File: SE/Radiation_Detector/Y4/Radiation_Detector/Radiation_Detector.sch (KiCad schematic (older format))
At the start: 12 parts, among them IC1 MICROFJ-60035-TSV-TR1, J1 Bus

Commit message: changed it so that there was 1 more level of heigherarchy now it's the top level with the bus connected to the bias and 4 detectors
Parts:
- removed C2: 10 nF (HV), symbol 001:C
- removed C3: 1 uF, symbol 001:C
- removed IC1: MICROFJ-60035-TSV-TR1, SS:SiPM_BGA36C100P6X6_613X613X67, symbol SS:MICROFJ-60035-TSV-TR1
- removed R6: 1 k, symbol Device:R_US
- removed R7: 108 k, symbol Device:R_US
- J1: symbol SS:Bus -> Radiation_Detector-rescue:Bus-SS
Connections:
- net labels removed: PS-A2D
- wire segments 125 -> 52
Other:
- note added: "Det_1"
- note added: "Det_2"
- note added: "Det_3"
- note added: "Det_4\n"
- note removed: "Charge\nSensitive\nPreamplifier"
- note removed: "Pulse\nShaper"
- note removed: "SiPM"

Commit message: incorporated A2D with SiPM, main work continueing from here is the Detector schematic and maybe the A2D references. in the Detector the SiPM needs to be changed to the Broadcom SiPM and the CSP needs to be the redesigned one and the PS needs to be designed so that we can redesign the Cremat one
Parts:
- J1: symbol Radiation_Detector-rescue:Bus-SS -> SS:Bus
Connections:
- wire segments 52 -> 56
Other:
- note added: "A2D_1"
- note added: "A2D_2\n"
- note added: "A2D_3"
- note added: "A2D_4"
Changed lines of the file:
@@
 $Descr A4 11693 8268
 encoding utf-8
-Sheet 1 4
+Sheet 1 17
 Title ""
 Date ""
@@
 $EndDescr
 $Comp
-L Radiation_Detector-rescue:Bus-SS J1
+L SS:Bus J1
 U 1 1 5EBBBD0C
 P 1350 2000
@@
 S 4850 800  1050 800
 U 5EBD2B15
-F0 "Detector_1" 50
-F1 "Detector_1.sch" 50
+F0 "Det_1" 50
+F1 "Detector.sch" 50
 F2 "+30V_Bias" I L 4850 1000 50
 F3 "+8V" I L 4850 1200 50
@@
 Text Notes 5100 1250 0    100  ~ 20
 Det_1
+Text Notes 5100 2250 0    100  ~ 20
+Det_2
+Text Notes 5100 3250 0    100  ~ 20
+Det_3
+Text Notes 5100 4250 0    100  ~ 20
+Det_4\n
+Connection ~ 4250 1000
+Wire Wire Line
+	4250 1000 4250 1200
+Wire Wire Line
+	4450 1000 4450 2000
+Connection ~ 4450 1000
+Wire Wire Line
+	4450 1000 4250 1000
+Connection ~ 4450 3000
+Wire Wire Line
+	4450 3000 4450 4000
+Connection ~ 4450 2000
+Wire Wire Line
+	4450 2000 4450 3000
+Text GLabel 4750 1200 0    50   Input ~ 0
++8V
+Wire Wire Line
+	4450 1000 4850 1000
+Wire Wire Line
+	4850 1200 4750 1200
+Text GLabel 4750 1400 0    50   Input ~ 0
+GND
+Wire Wire Line
+	4750 1400 4850 1400
+Wire Wire Line
+	4450 2000 4850 2000
+Wire Wire Line
+	4450 3000 4850 3000
+Wire Wire Line
+	4450 4000 4850 4000
+Text GLabel 4750 2200 0    50   Input ~ 0
++8V
+Wire Wire Line
+	4850 2200 4750 2200
+Text GLabel 4750 2400 0    50   Input ~ 0
+GND
+Wire Wire Line
+	4750 2400 4850 2400
+Text GLabel 4750 3200 0    50   Input ~ 0
++8V
+Wire Wire Line
+	4850 3200 4750 3200
+Text GLabel 4750 3400 0    50   Input ~ 0
+GND
+Wire Wire Line
+	4750 3400 4850 3400
+Text GLabel 4750 4200 0    50   Input ~ 0
++8V
+Wire Wire Line
+	4850 4200 4750 4200
+Text GLabel 4750 4400 0    50   Input ~ 0
+GND
+Wire Wire Line
+	4750 4400 4850 4400
 $Sheet
 S 4850 1800 1050 800
-U 5EC023EE
-F0 "sheet5EC023E8" 50
-F1 "Detector_1.sch" 50
+U 5EC10E33
+F0 "Det_2" 50
+F1 "Detector.sch" 50
 F2 "+30V_Bias" I L 4850 2000 50
 F3 "+8V" I L 4850 2200 50
@@
 F5 "PS-A2D" I R 5900 2200 50
 $EndSheet
-Text Notes 5100 2250 0    100  ~ 20
-Det_2
 $Sheet
 S 4850 2800 1050 800
-U 5EC027A1
-F0 "sheet5EC0279B" 50
-F1 "Detector_1.sch" 50
+U 5EC116B0
+F0 "Det_3" 50
+F1 "Detector.sch" 50
 F2 "+30V_Bias" I L 4850 3000 50
 F3 "+8V" I L 4850 3200 50
@@
 F5 "PS-A2D" I R 5900 3200 50
 $EndSheet
-Text Notes 5100 3250 0    100  ~ 20
-Det_3
 $Sheet
 S 4850 3800 1050 800
-U 5EC02B54
-F0 "sheet5EC02B4E" 50
-F1 "Detector_1.sch" 50
+U 5EC11F15
+F0 "Det_4" 50
+F1 "Detector.sch" 50
 F2 "+30V_Bias" I L 4850 4000 50
 F3 "+8V" I L 4850 4200 50
@@
 F5 "PS-A2D" I R 5900 4200 50
 $EndSheet
-Text Notes 5100 4250 0    100  ~ 20
-Det_4\n
-Connection ~ 4250 1000
-Wire Wire Line
-	4250 1000 4250 1200
-Wire Wire Line
-	4450 1000 4450 2000
-Connection ~ 4450 1000
-Wire Wire Line
-	4450 1000 4250 1000
-Connection ~ 4450 3000
-Wire Wire Line
-	4450 3000 4450 4000
-Connection ~ 4450 2000
-Wire Wire Line
-	4450 2000 4450 3000
-Text GLabel 4750 1200 0    50   Input ~ 0
-+8V
-Wire Wire Line
-	4450 1000 4850 1000
-Wire Wire Line
-	4850 1200 4750 1200
-Text GLabel 4750 1400 0    50   Input ~ 0
-GND
-Wire Wire Line
-	4750 1400 4850 1400
-Wire Wire Line
-	4450 2000 4850 2000
-Wire Wire Line
-	4450 3000 4850 3000
-Wire Wire Line
-	4450 4000 4850 4000
-Text GLabel 4750 2200 0    50   Input ~ 0
-+8V
-Wire Wire Line
-	4850 2200 4750 2200
-Text GLabel 4750 2400 0    50   Input ~ 0
-GND
-Wire Wire Line
-	4750 2400 4850 2400
-Text GLabel 4750 3200 0    50   Input ~ 0
-+8V
-Wire Wire Line
-	4850 3200 4750 3200
-Text GLabel 4750 3400 0    50   Input ~ 0
-GND
-Wire Wire Line
-	4750 3400 4850 3400
-Text GLabel 4750 4200 0    50   Input ~ 0
-+8V
-Wire Wire Line
-	4850 4200 4750 4200
-Text GLabel 4750 4400 0    50   Input ~ 0
-GND
-Wire Wire Line
-	4750 4400 4850 4400
+$Sheet
+S 6100 1100 1100 700
+U 5EBDE6C5
+F0 "A2D_1" 50
+F1 "A2D.sch" 50
+F2 "PS-A2D" I L 6100 1200 50
+F3 "S1" I R 7200 1600 50
+F4 "S2" I R 7200 1500 50
+F5 "!CLR" I R 7200 1400 50
+F6 "Reset" I R 7200 1300 50
+F7 "A2D_Out" I R 7200 1200 50
+F8 "CLK" I R 7200 1700 50
+$EndSheet
+Text Notes 6300 1500 0    100  ~ 20
+A2D_1
+$Sheet
+S 6100 2100 1100 700
+U 5EBF5005
+F0 "A2D_2" 50
+F1 "A2D.sch" 50
+F2 "PS-A2D" I L 6100 2200 50
+F3 "S1" I R 7200 2600 50
+F4 "S2" I R 7200 2500 50
+F5 "!CLR" I R 7200 2400 50
+F6 "Reset" I R 7200 2300 50
+F7 "A2D_Out" I R 7200 2200 50
+F8 "CLK" I R 7200 2700 50
+$EndSheet
+Text Notes 6300 2500 0    100  ~ 20
+A2D_2\n
+$Sheet
+S 6100 3100 1100 700
+U 5EBF586D
+F0 "A2D_3" 50
+F1 "A2D.sch" 50
+F2 "PS-A2D" I L 6100 3200 50
+F3 "S1" I R 7200 3600 50
+F4 "S2" I R 7200 3500 50
+F5 "!CLR" I R 7200 3400 50
+F6 "Reset" I R 7200 3300 50
+F7 "A2D_Out" I R 7200 3200 50
+F8 "CLK" I R 7200 3700 50
+$EndSheet
+Text Notes 6300 3500 0    100  ~ 20
+A2D_3
+Text Notes 6300 4500 0    100  ~ 20
+A2D_4
+Wire Wire Line
+	5900 1200 6100 1200
+Wire Wire Line
+	5900 2200 6100 2200
+Wire Wire Line
+	5900 3200 6100 3200
+Wire Wire Line
+	5900 4200 6100 4200
+$Sheet
+S 6100 4100 1100 700
+U 5EBF60D5
+F0 "A2D_4" 50
+F1 "A2D.sch" 50
+F2 "PS-A2D" I L 6100 4200 50
+F3 "S1" I R 7200 4600 50
+F4 "S2" I R 7200 4500 50
+F5 "!CLR" I R 7200 4400 50
+F6 "Reset" I R 7200 4300 50
+F7 "A2D_Out" I R 7200 4200 50
+F8 "CLK" I R 7200 4700 50
+$EndSheet
 $EndSCHEMATC

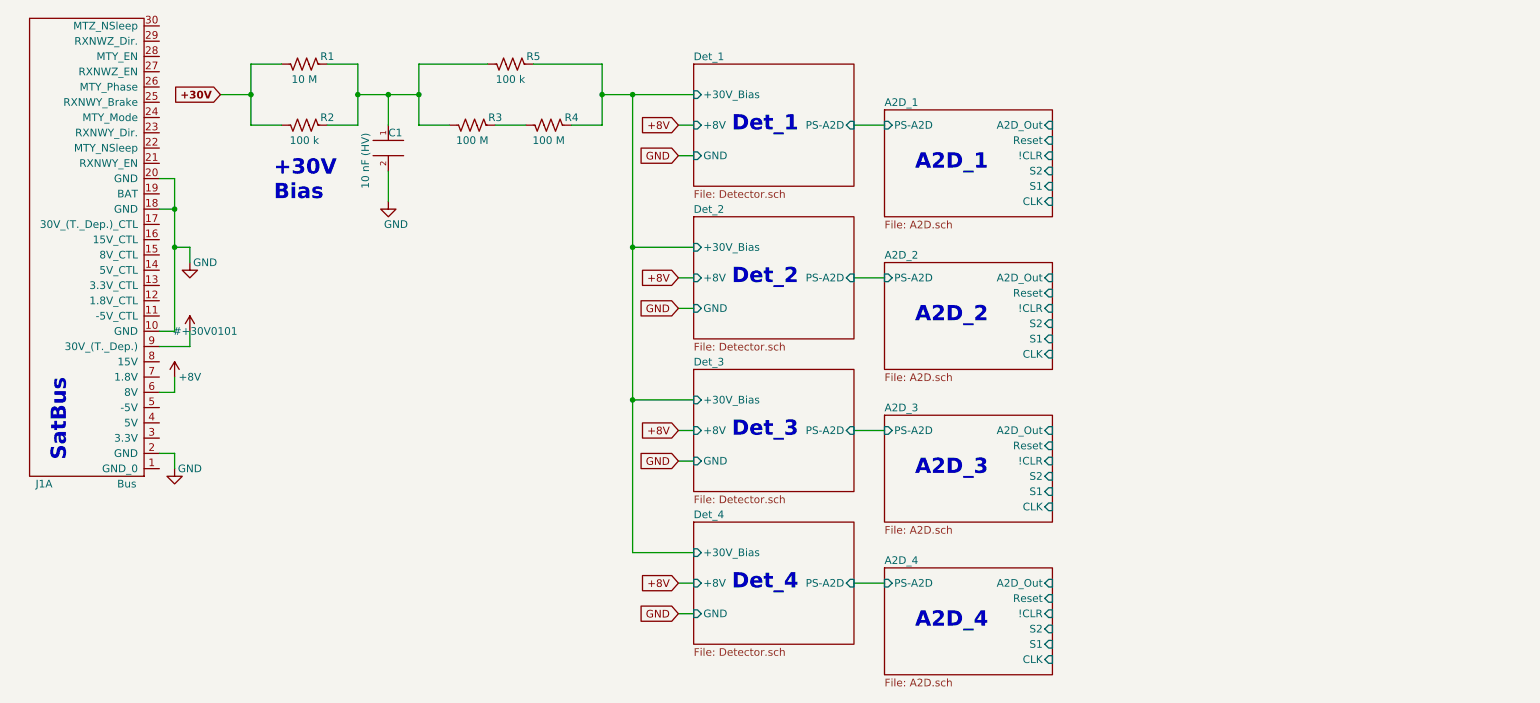
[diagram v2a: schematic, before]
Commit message: top level schematic pre-design review. after feedback from Petersen there is much to change specifically in the A2D section
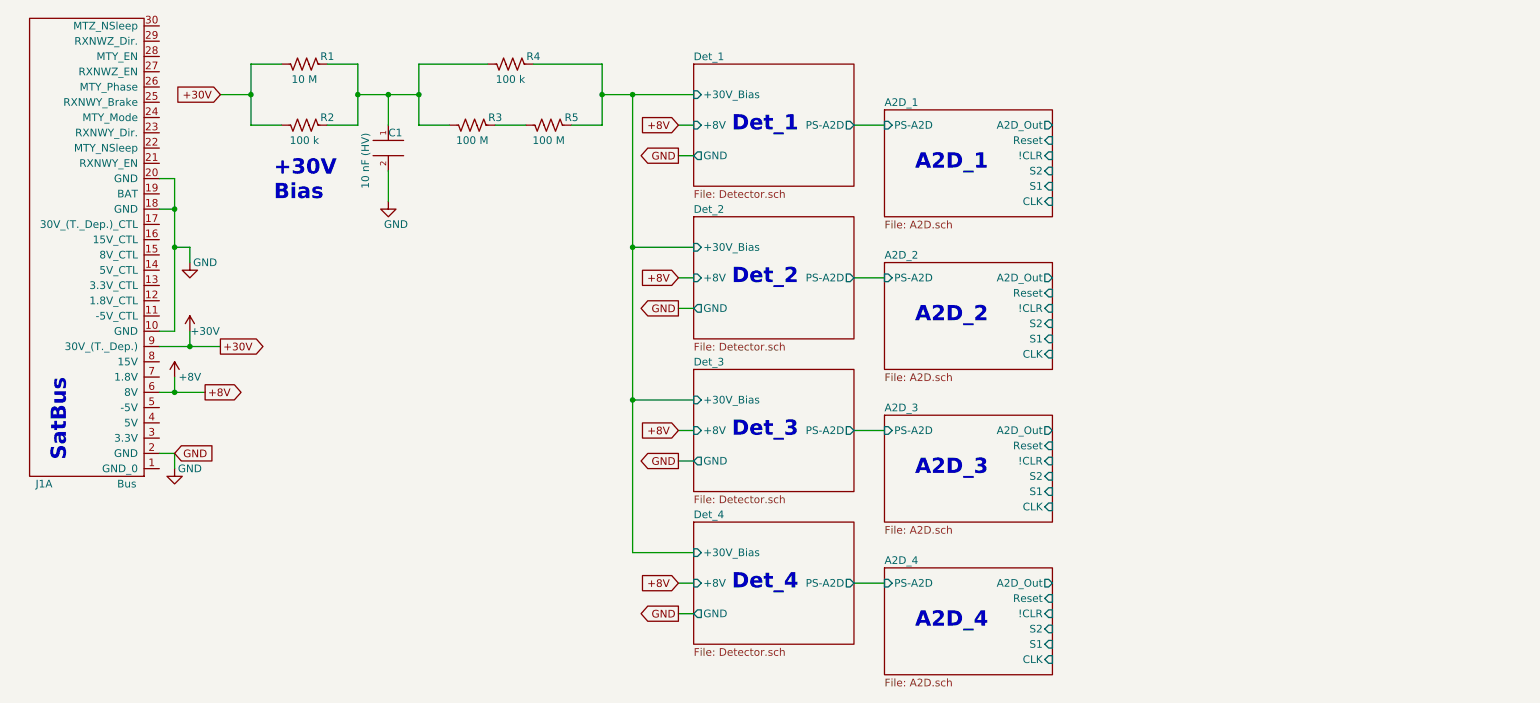
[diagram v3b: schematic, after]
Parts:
- added +30V: +36V, symbol power:+36V
- renumbered R5 to R4, R4 to R5
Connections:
- net +30V is gone; now on net +36V: R1.1, R2.1
- net +36V: now also +30V.1 (+36V)
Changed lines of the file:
@@
 EESchema Schematic File Version 4
-LIBS:Radiation_Detector-cache
 EELAYER 26 0
 EELAYER END
@@
 $EndComp
 $Comp
-L power:+36V #+30V0101
+L power:+36V +30V
 U 1 1 5EBBBD77
 P 1550 2550
-F 0 "#+30V0101" H 1650 2550 50  0000 C CNN
+F 0 "+30V" H 1650 2550 50  0000 C CNN
 F 1 "+36V" H 1650 2500 50  0001 C CNN
 F 2 "" H 1550 2550 50  0001 C CNN
@@
 $EndComp
 $Comp
-L power:GND #PWR0101
+L power:GND #PWR02
 U 1 1 5EBBBDA4
 P 1450 3450
-F 0 "#PWR0101" H 1450 3200 50  0001 C CNN
+F 0 "#PWR02" H 1450 3200 50  0001 C CNN
 F 1 "GND" H 1550 3450 50  0000 C CNN
 F 2 "" H 1450 3450 50  0001 C CNN
@@
 	1350 3350 1450 3350
 $Comp
-L power:GND #PWR0102
+L power:GND #PWR03
 U 1 1 5EBBC3CE
 P 1550 2100
-F 0 "#PWR0102" H 1550 1850 50  0001 C CNN
+F 0 "#PWR03" H 1550 1850 50  0001 C CNN
 F 1 "GND" H 1650 2100 50  0000 C CNN
 F 2 "" H 1550 2100 50  0001 C CNN
@@
 $EndComp
 $Comp
-L power:GND #PWR0105
+L power:GND #PWR04
 U 1 1 5EC06ECC
 P 2850 1700
-F 0 "#PWR0105" H 2850 1450 50  0001 C CNN
+F 0 "#PWR04" H 2850 1450 50  0001 C CNN
 F 1 "GND" H 2900 1550 50  0000 C CNN
 F 2 "" H 2850 1700 50  0001 C CNN
@@
 $EndComp
 $Comp
-L Device:R_US R5
+L Device:R_US R4
 U 1 1 5EC0AF9F
 P 3650 800
-F 0 "R5" V 3700 950 50  0000 C CNN
+F 0 "R4" V 3700 950 50  0000 C CNN
 F 1 "100 k" V 3550 800 50  0000 C CNN
 F 2 "" V 3690 790 50  0001 C CNN
@@
 $EndComp
 $Comp
-L Device:R_US R4
+L Device:R_US R5
 U 1 1 5EC0D1F1
 P 3900 1200
-F 0 "R4" V 3950 1350 50  0000 C CNN
+F 0 "R5" V 3950 1350 50  0000 C CNN
 F 1 "100 M" V 3800 1200 50  0000 C CNN
 F 2 "" V 3940 1190 50  0001 C CNN
@@
 $EndComp
 $Comp
-L power:+8V #PWR0106
+L power:+8V #PWR01
 U 1 1 5EC1EDB2
 P 1450 2850
-F 0 "#PWR0106" H 1450 2700 50  0001 C CNN
+F 0 "#PWR01" H 1450 2700 50  0001 C CNN
 F 1 "+8V" H 1550 2850 50  0000 C CNN
 F 2 "" H 1450 2850 50  0001 C CNN
@@
 Text Notes 2100 1700 0    100  ~ 20
 +30V\nBias
-Text GLabel 1750 1000 0    50   Input ~ 10
+Text GLabel 1750 1000 0    50   Input ~ 0
 +30V
 Wire Wire Line
@@
 F2 "+30V_Bias" I L 4850 1000 50
 F3 "+8V" I L 4850 1200 50
-F4 "GND" I L 4850 1400 50
-F5 "PS-A2D" I R 5900 1200 50
+F4 "GND" O L 4850 1400 50
+F5 "PS-A2D" O R 5900 1200 50
 $EndSheet
 Text Notes 5100 1250 0    100  ~ 20
@@
 Wire Wire Line
 	4850 1200 4750 1200
-Text GLabel 4750 1400 0    50   Input ~ 0
+Text GLabel 4750 1400 0    50   Output ~ 0
 GND
 Wire Wire Line
@@
 Wire Wire Line
 	4850 2200 4750 2200
-Text GLabel 4750 2400 0    50   Input ~ 0
+Text GLabel 4750 2400 0    50   Output ~ 0
 GND
 Wire Wire Line
@@
 Wire Wire Line
 	4850 3200 4750 3200
-Text GLabel 4750 3400 0    50   Input ~ 0
+Text GLabel 4750 3400 0    50   Output ~ 0
 GND
 Wire Wire Line
@@
 Wire Wire Line
 	4850 4200 4750 4200
-Text GLabel 4750 4400 0    50   Input ~ 0
+Text GLabel 4750 4400 0    50   Output ~ 0
 GND
 Wire Wire Line
 	4750 4400 4850 4400
-$Sheet
-S 4850 1800 1050 800
-U 5EC10E33
-F0 "Det_2" 50
-F1 "Detector.sch" 50
-F2 "+30V_Bias" I L 4850 2000 50
-F3 "+8V" I L 4850 2200 50
-F4 "GND" I L 4850 2400 50
-F5 "PS-A2D" I R 5900 2200 50
-$EndSheet
 $Sheet
 S 4850 2800 1050 800
@@
 F2 "+30V_Bias" I L 4850 3000 50
 F3 "+8V" I L 4850 3200 50
-F4 "GND" I L 4850 3400 50
-F5 "PS-A2D" I R 5900 3200 50
+F4 "GND" O L 4850 3400 50
+F5 "PS-A2D" O R 5900 3200 50
 $EndSheet
 $Sheet
@@
 F2 "+30V_Bias" I L 4850 4000 50
 F3 "+8V" I L 4850 4200 50
-F4 "GND" I L 4850 4400 50
-F5 "PS-A2D" I R 5900 4200 50
+F4 "GND" O L 4850 4400 50
+F5 "PS-A2D" O R 5900 4200 50
 $EndSheet
 $Sheet
@@
 F5 "!CLR" I R 7200 1400 50
 F6 "Reset" I R 7200 1300 50
-F7 "A2D_Out" I R 7200 1200 50
-F8 "CLK" I R 7200 1700 50
+F7 "CLK" I R 7200 1700 50
+F8 "A2D_Out" O R 7200 1200 50
 $EndSheet
 Text Notes 6300 1500 0    100  ~ 20
@@
 F5 "!CLR" I R 7200 2400 50
 F6 "Reset" I R 7200 2300 50
-F7 "A2D_Out" I R 7200 2200 50
-F8 "CLK" I R 7200 2700 50
+F7 "CLK" I R 7200 2700 50
+F8 "A2D_Out" O R 7200 2200 50
 $EndSheet
 Text Notes 6300 2500 0    100  ~ 20
@@
 F5 "!CLR" I R 7200 3400 50
 F6 "Reset" I R 7200 3300 50
-F7 "A2D_Out" I R 7200 3200 50
-F8 "CLK" I R 7200 3700 50
+F7 "CLK" I R 7200 3700 50
+F8 "A2D_Out" O R 7200 3200 50
 $EndSheet
 Text Notes 6300 3500 0    100  ~ 20
@@
 F5 "!CLR" I R 7200 4400 50
 F6 "Reset" I R 7200 4300 50
-F7 "A2D_Out" I R 7200 4200 50
-F8 "CLK" I R 7200 4700 50
-$EndSheet
+F7 "CLK" I R 7200 4700 50
+F8 "A2D_Out" O R 7200 4200 50
+$EndSheet
+Text GLabel 1750 2650 2    50   Output ~ 0
++30V
+Wire Wire Line
+	1750 2650 1550 2650
+Connection ~ 1550 2650
+Text GLabel 1650 2950 2    50   Output ~ 0
++8V
+Wire Wire Line
+	1450 2950 1650 2950
+Connection ~ 1450 2950
+$Sheet
+S 4850 1800 1050 800
+U 5EC10E33
+F0 "Det_2" 50
+F1 "Detector.sch" 50
+F2 "+30V_Bias" I L 4850 2000 50
+F3 "+8V" I L 4850 2200 50
+F4 "GND" O L 4850 2400 50
+F5 "PS-A2D" O R 5900 2200 50
+$EndSheet
+Text GLabel 1450 3350 2    50   Input ~ 0
+GND
 $EndSCHEMATC

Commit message: lots of A2D changes plus new folder for LT Spice Sim
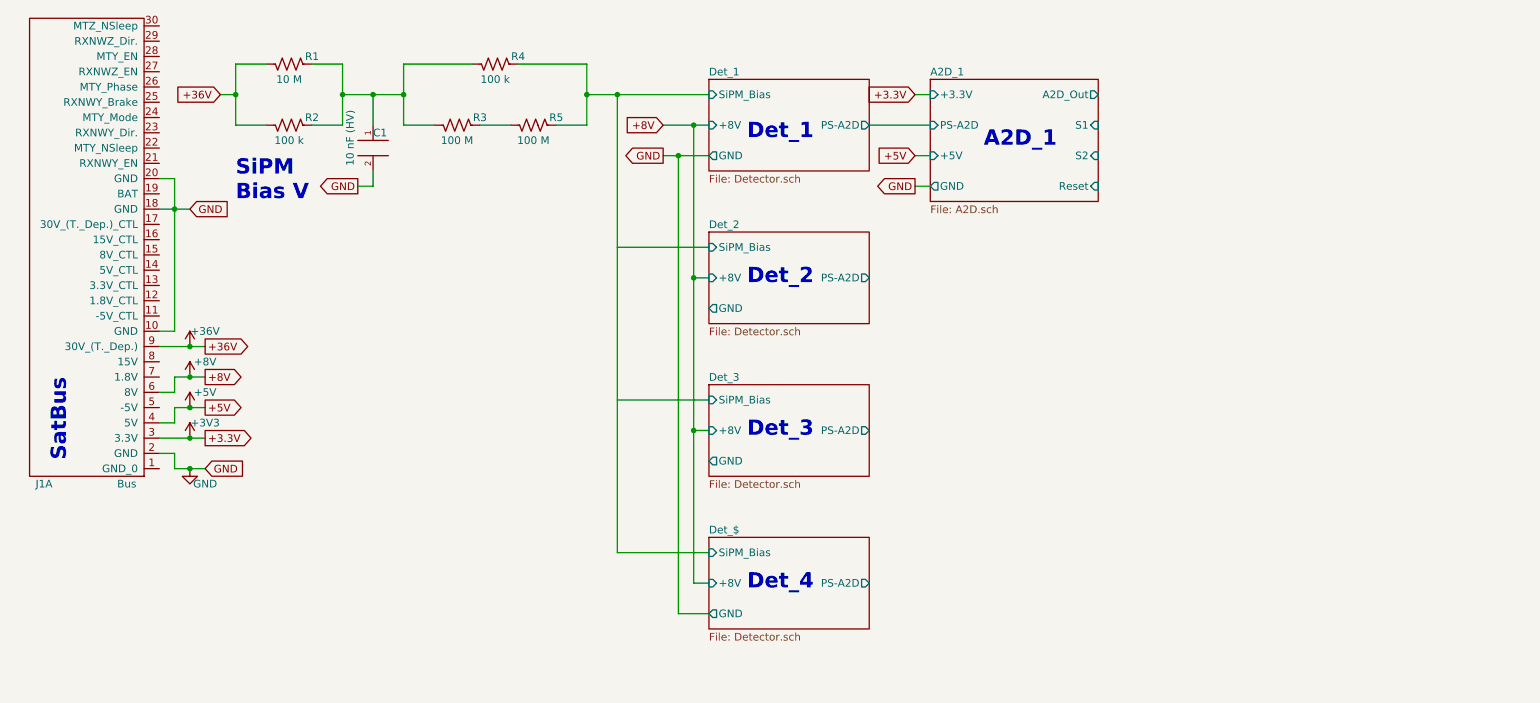
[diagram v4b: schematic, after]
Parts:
- removed +30V: +36V, symbol power:+36V
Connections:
- net labels added: +3.3V, +36V, +3V3, +5V
- net labels removed: +30V
- wire segments 58 -> 67
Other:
- note added: "SiPM\nBias V"
- note removed: "+30V\nBias"
- note removed: "A2D_2\n"
- note removed: "A2D_3"
- note removed: "A2D_4"
- moved on the sheet: C1, R1, R2, R3, R4, R5

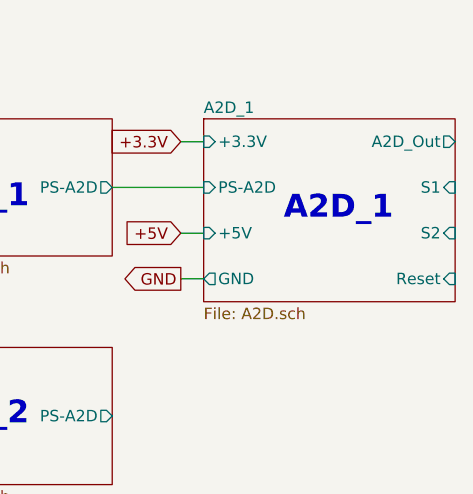
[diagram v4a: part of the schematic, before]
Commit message: finished up A2D stuff and OR stuff whats left is updating the bus to reflect the old v0.4 from Winter and then ORing the outputs at the high level for the ISR and reconnecting the ISR, DATA, selector etc back to the Bus
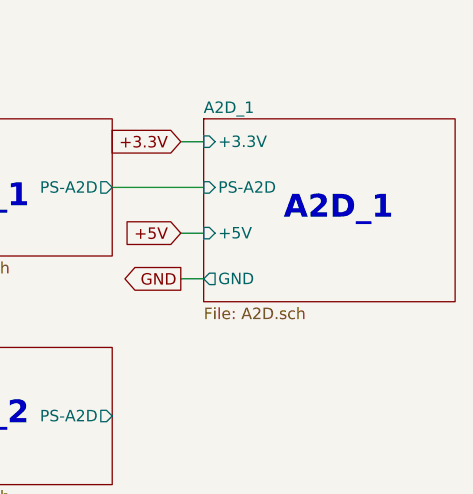
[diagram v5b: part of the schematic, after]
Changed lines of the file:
@@
 F3 "+5V" I L 6400 1400 50
 F4 "GND" O L 6400 1600 50
-F5 "S1" I R 7500 1200 50
-F6 "S2" I R 7500 1400 50
-F7 "Reset" I R 7500 1600 50
-F8 "A2D_Out" O R 7500 1000 50
-F9 "+3.3V" I L 6400 1000 50
+F5 "+3.3V" I L 6400 1000 50
 $EndSheet
 Text Notes 6750 1350 0    100  ~ 20
